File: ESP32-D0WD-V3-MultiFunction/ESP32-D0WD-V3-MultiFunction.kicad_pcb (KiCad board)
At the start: 2 copper layers, 104.1 x 127 mm, 144 parts, among them J201 Programming Header, J801 RJ45, J802 RJ45, P701 A7 A6 A5 A4 A3 A2 A1 A0 C, P702 B7 B6 B5 B4 B3 B2 B1 B0 C, SW201 RESET, T701 + 12V -, T801 - 15 in +, T802 - 15 out +, U201 ESP32-D0WD-V3, U202 W25Q32JVSSIQ, U301 LM2574N-3.3, U401 TC4426, U402 TC4426, U403 74HCT14, U501 74HCT00, U502 74HCT00, U503 TC4428, U504 TC4428, U505 TC4428, U506 TC4428, U601 LM339, U602 LM339, U701 PCA9685, U702 TBD62X83A, U703 TBD62X83A, U801 TCAN332DR, Y201 40 Mhz +/- 10 ppm

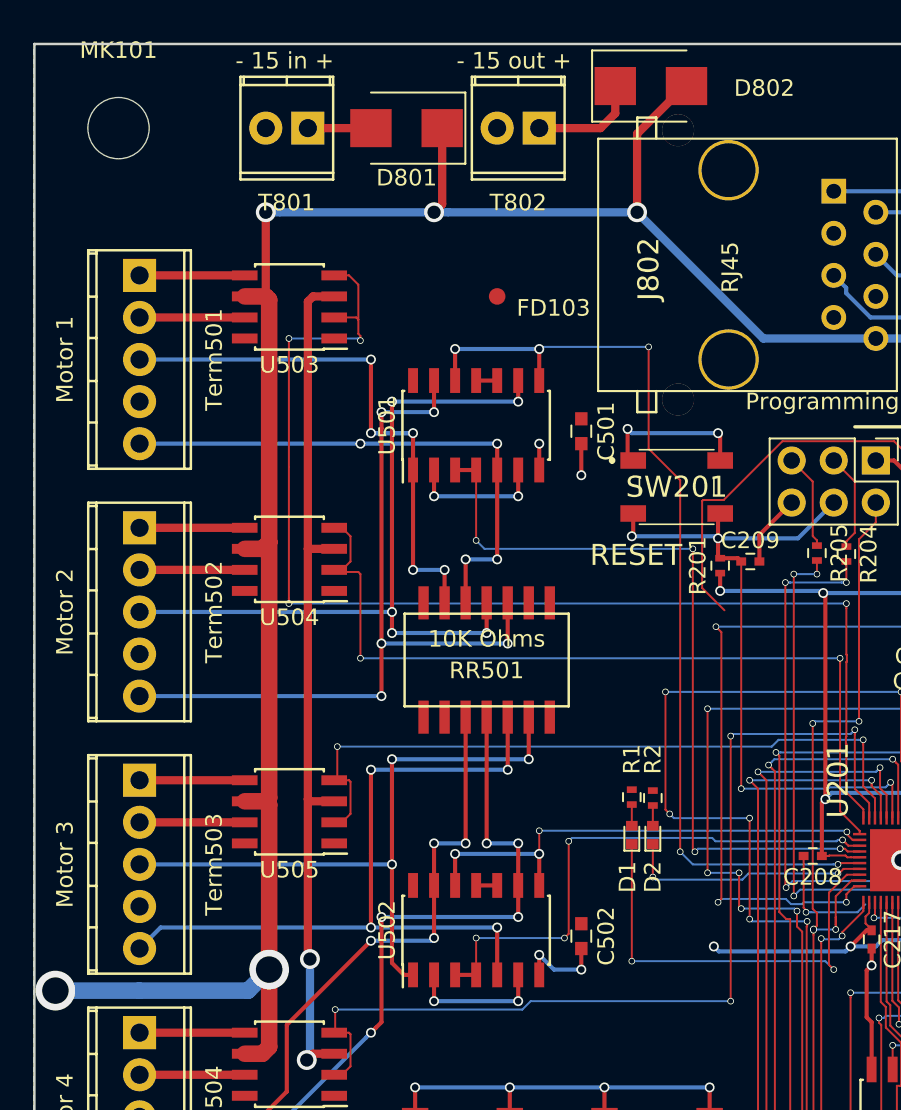
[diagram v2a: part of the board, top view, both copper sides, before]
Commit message: Complete BOM for ESP32-D0WD-V3-MultiFunction.
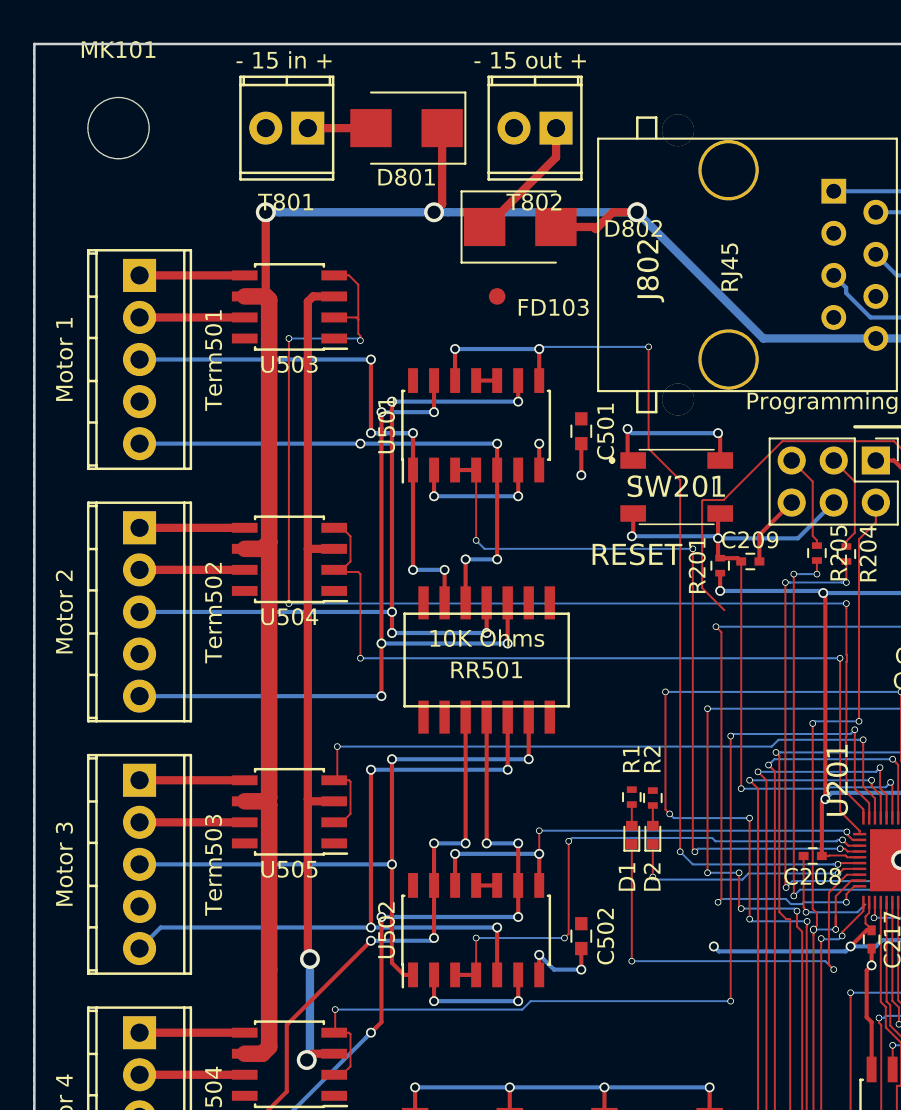
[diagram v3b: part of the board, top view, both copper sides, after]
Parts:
- moved D802 11.6 mm to (105.5, 36.4)
- moved T802 1.02 mm to (107.7, 30.5)
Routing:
- net CAN +12V: track 366.8 -> 350.2 mm, vias 13 -> 11
- net Net-(D802-Pad1): track 6.61 -> 7.81 mm
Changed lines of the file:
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@@
     (thickness 1.6)
     (drawings 17)
-    (tracks 1999)
+    (tracks 1995)
     (zones 0)
     (modules 144)
@@
     (47 F.CrtYd user)
     (48 B.Fab user)
-    (49 F.Fab user hide)
+    (49 F.Fab user)
   )
   (setup
-    (last_trace_width 0.25)
+    (last_trace_width 0.5)
     (user_trace_width 0.12)
     (user_trace_width 0.5)
@@
   )
   (module Diodes_SMD:D_SMB (layer F.Cu)
-    (at 113.42 27.94)
+    (at 105.537 36.449)
     (descr "Diode SMB (DO-214AA)")
     (tags "Diode SMB (DO-214AA)")
@@
   )
   (module Connectors_Terminal_Blocks:TerminalBlock_Pheonix_MPT-2.54mm_2pol (layer F.Cu)
-    (at 106.68 30.48 180)
+    (at 107.696 30.48 180)
     (descr "2-way 2.54mm pitch terminal block, Phoenix MPT series")
     (fp_text reference T802 (at 1.27 -4.50088 180) (layer F.SilkS)
@@
   (segment (start 135.714 75.946) (end 135.714 76.108) (width 0.25) (layer F.Cu) (net 10))
   (segment (start 135.714 76.108) (end 136.06 76.454) (width 0.25) (layer F.Cu) (net 10))
+  (segment (start 110.1 36.576) (end 109.973 36.449) (width 0.5) (layer F.Cu) (net 11))
+  (segment (start 109.973 36.449) (end 107.687 36.449) (width 0.5) (layer F.Cu) (net 11))
+  (segment (start 112.586988 35.56) (end 111.116 35.56) (width 0.5) (layer F.Cu) (net 11))
+  (segment (start 111.116 35.56) (end 110.1 36.576) (width 0.5) (layer F.Cu) (net 11))
   (segment (start 90.17 71.12) (end 88.9 71.12) (width 1) (layer F.Cu) (net 11))
   (segment (start 100.33 35.56) (end 101.178528 35.56) (width 0.5) (layer B.Cu) (net 11))
@@
   (segment (start 100.82 35.07) (end 100.33 35.56) (width 0.5) (layer F.Cu) (net 11))
   (via (at 100.33 35.56) (size 1.2) (drill 0.8) (layers F.Cu B.Cu) (net 11))
-  (segment (start 115.57 27.94) (end 115.47 27.94) (width 0.5) (layer F.Cu) (net 11))
-  (segment (start 115.47 27.94) (end 112.586988 30.823012) (width 0.5) (layer F.Cu) (net 11))
-  (segment (start 112.586988 30.823012) (end 112.586988 35.17651) (width 0.5) (layer F.Cu) (net 11))
   (via (at 112.586988 35.56) (size 1.2) (drill 0.8) (layers F.Cu B.Cu) (net 11))
   (segment (start 112.586988 35.17651) (end 112.586988 35.56) (width 0.5) (layer F.Cu) (net 11))
@@
   (segment (start 127 43.18) (end 148.59 43.18) (width 0.5) (layer B.Cu) (net 11))
   (via (at 148.59 43.18) (size 1.2) (drill 0.8) (layers F.Cu B.Cu) (net 11))
-  (segment (start 90.375001 81.28) (end 89.105001 82.55) (width 1) (layer B.Cu) (net 11))
-  (segment (start 89.105001 82.55) (end 82.525248 82.55) (width 1) (layer B.Cu) (net 11))
-  (segment (start 82.525248 82.55) (end 77.47 82.55) (width 1) (layer B.Cu) (net 11))
-  (via (at 77.47 82.55) (size 2.4) (drill 1.6) (layers F.Cu B.Cu) (net 11))
   (segment (start 90.375001 81.28) (end 90.375001 85.950001) (width 1) (layer F.Cu) (net 11))
   (segment (start 90.375001 71.325001) (end 90.375001 81.28) (width 1) (layer F.Cu) (net 11))
-  (via (at 90.375001 81.28) (size 2.4) (drill 1.6) (layers F.Cu B.Cu) (net 11))
   (segment (start 90.17 71.12) (end 90.375001 71.325001) (width 1) (layer F.Cu) (net 11))
   (segment (start 90.375001 85.950001) (end 89.965002 86.36) (width 1) (layer F.Cu) (net 11))
@@
   (segment (start 173.99 88.41) (end 173.99 85.09) (width 0.5) (layer F.Cu) (net 37))
   (segment (start 92.71 30.48) (end 96.52 30.48) (width 0.5) (layer F.Cu) (net 38))
-  (segment (start 106.68 30.48) (end 110.38 30.48) (width 0.5) (layer F.Cu) (net 39))
-  (segment (start 110.38 30.48) (end 111.27 29.59) (width 0.5) (layer F.Cu) (net 39))
-  (segment (start 111.27 29.59) (end 111.27 27.94) (width 0.5) (layer F.Cu) (net 39))
+  (segment (start 107.696 30.48) (end 107.696 32.24) (width 0.5) (layer F.Cu) (net 39))
+  (segment (start 107.696 32.24) (end 103.487 36.449) (width 0.5) (layer F.Cu) (net 39))
+  (segment (start 103.487 36.449) (end 103.387 36.449) (width 0.5) (layer F.Cu) (net 39))
   (segment (start 106.426 134.337158) (end 106.426 134.62) (width 0.12) (layer F.Cu) (net 40))
   (segment (start 105.537 132.08) (end 106.426 132.969) (width 0.12) (layer F.Cu) (net 40))

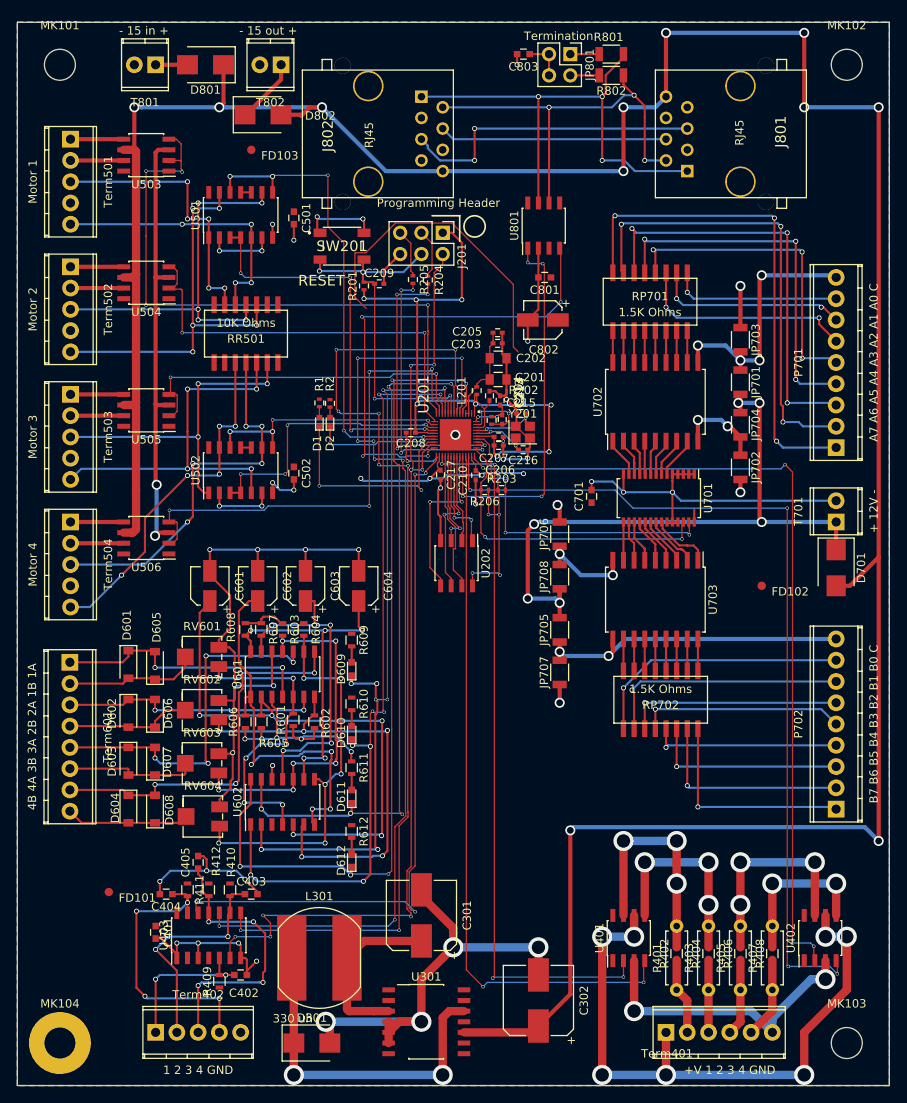
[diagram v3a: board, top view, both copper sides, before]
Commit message: Cosmetic updates: copyright, labels, etc.
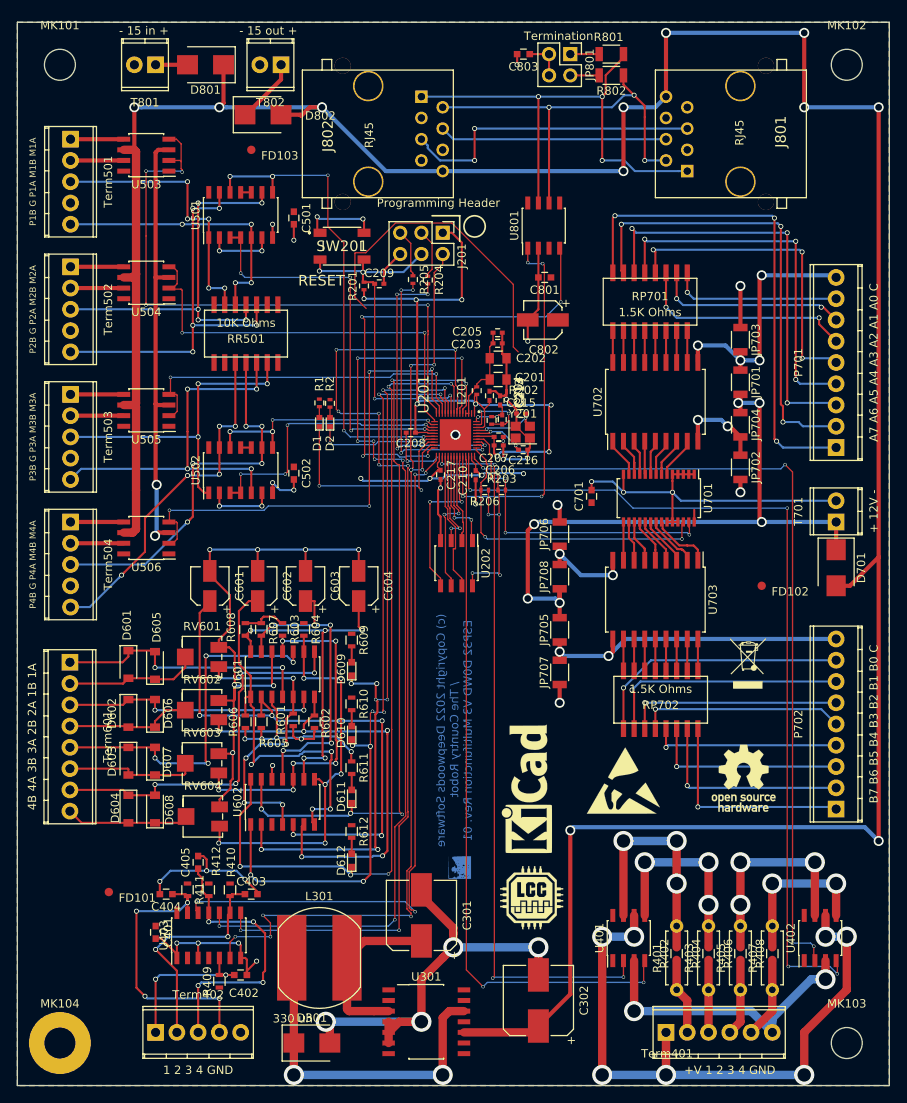
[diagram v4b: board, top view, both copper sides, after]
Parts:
- added ?: , DWSLogoBCU:DWSLogoBCU, F.Cu at (129.0, 126.4)
- added G***: LCC, LCC_LOGO:LCC_LOGO_9x9, F.Cu at (137.7, 129.9)
- added REF***: ESD-Logo_8.9x8mm_SilkScreen, Symbols:ESD-Logo_8.9x8mm_SilkScreen, F.Cu at (148.6, 116.0)
- added REF***: KiCad-Logo_6mm_SilkScreen, Symbols:KiCad-Logo_6mm_SilkScreen, F.Cu at (137.0, 117.0)
- added REF***: OSHW-Logo_7.5x8mm_SilkScreen, Symbols:OSHW-Logo_7.5x8mm_SilkScreen, F.Cu at (162.9, 115.7)
- added REF***: WEEE-Logo_4.2x6mm_SilkScreen, Symbols:WEEE-Logo_4.2x6mm_SilkScreen, F.Cu at (163.4, 102.0)
- Term501: value Motor 1 -> P1B G P1A M1B M1A
- Term502: value Motor 2 -> P2B G P2A M2B M2A
- Term503: value Motor 3 -> P3B G P3A M3B M3A
- Term504: value Motor 4 -> P4B G P4A M4B M4A
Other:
- board text added: "(c) Copyright 2022 Deepwoods Software / The Country Robot ESP32 D0WD V3 Multifunction Rev. 01"
